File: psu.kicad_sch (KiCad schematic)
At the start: 0 parts

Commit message: First version of analog path, without resistor values
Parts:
- added U16: DAC80504, Package_DFN_QFN:Texas_RTE0016D_WQFN-16-1EP_3x3mm_P0.5mm_EP0.8x0.8mm_ThermalVias, symbol Analog_DAC:DAC80504
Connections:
- new net CH1_GAIN_DAC: U16.2 (OUT0)
- new net CH1_OFFSET_DAC: U16.4 (OUT2)
- new net CH2_GAIN_DAC: U16.3 (OUT1)
- new net CH2_OFFSET_DAC: U16.5 (OUT3)

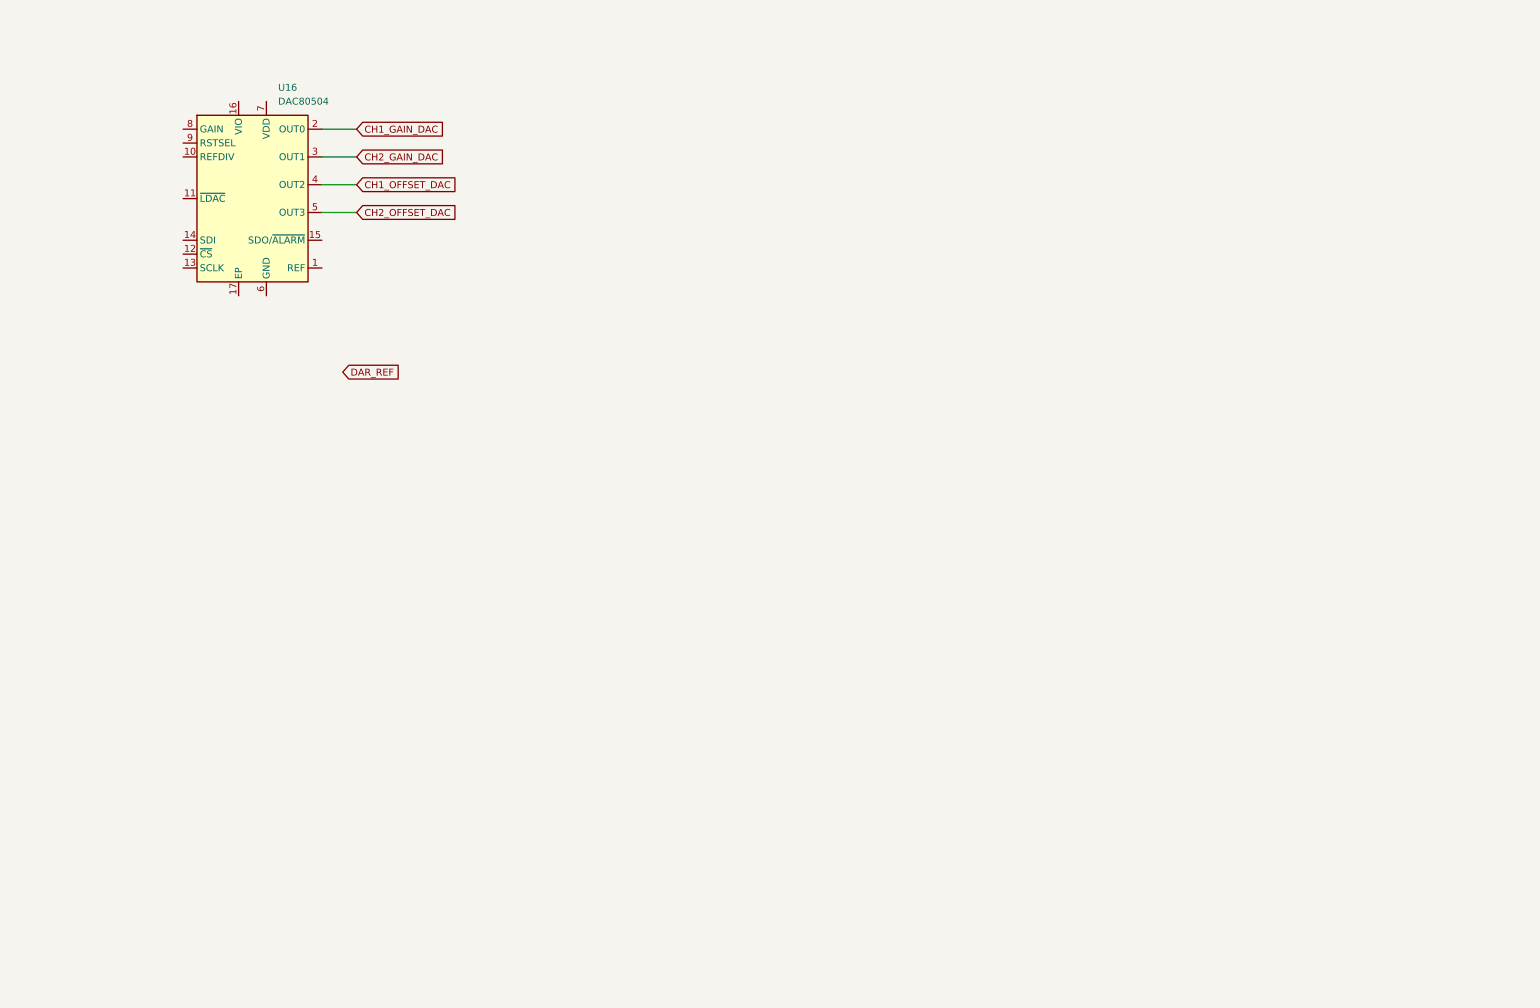
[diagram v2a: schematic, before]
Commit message: Touch up analog front end, add base of the psu
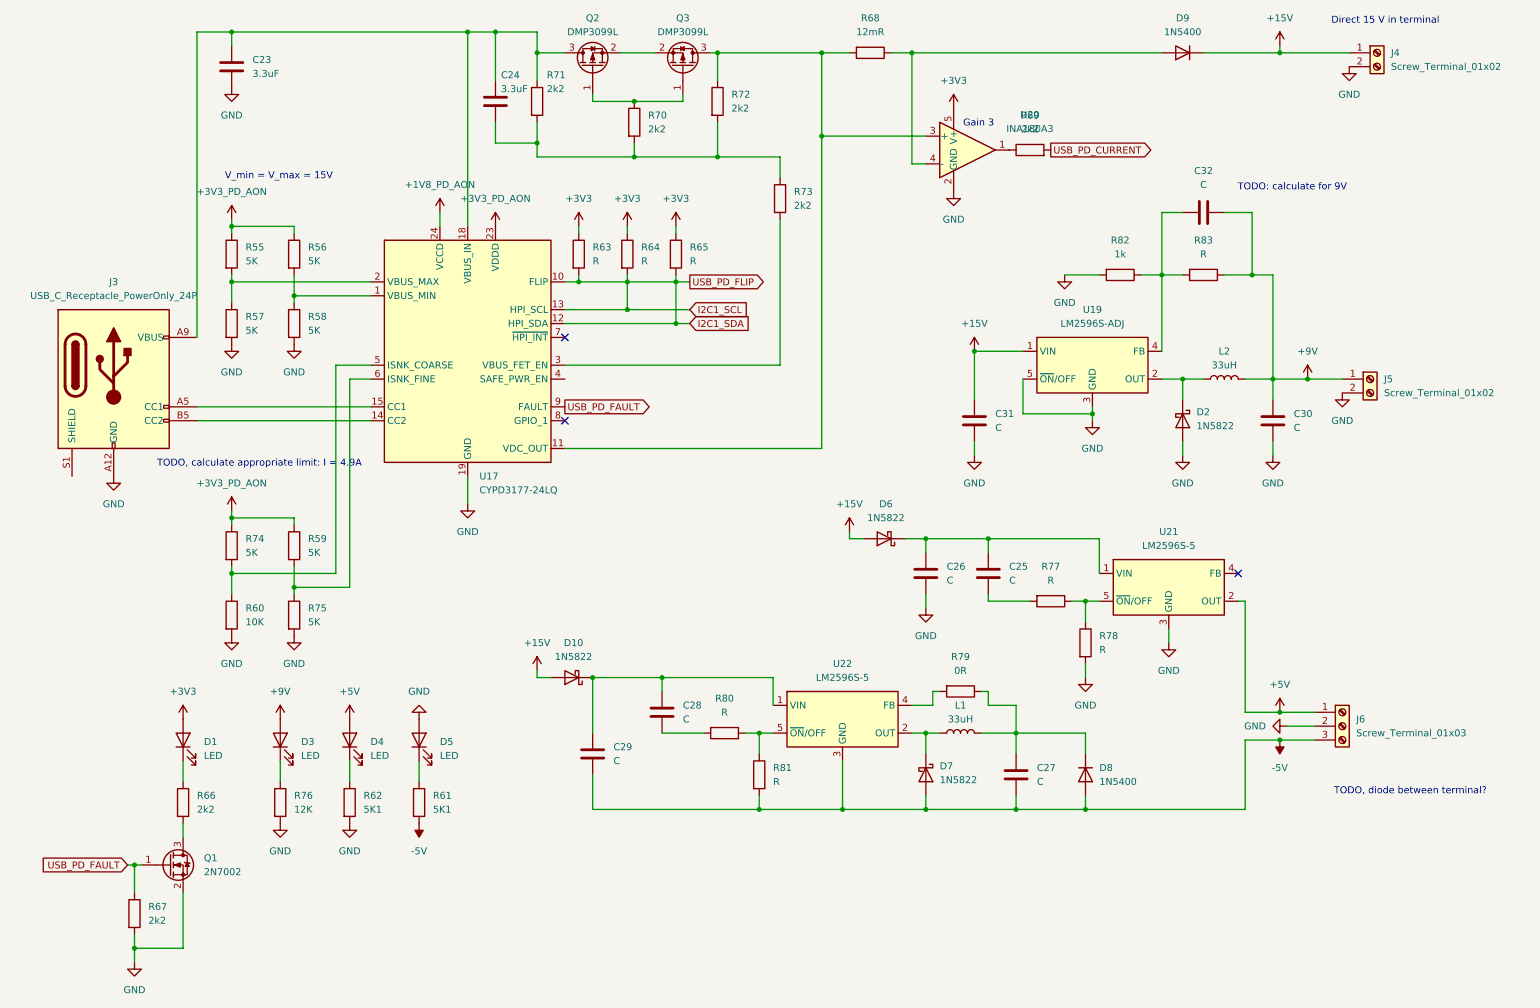
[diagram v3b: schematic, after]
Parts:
- removed U16: DAC80504, Package_DFN_QFN:Texas_RTE0016D_WQFN-16-1EP_3x3mm_P0.5mm_EP0.8x0.8mm_ThermalVias, symbol Analog_DAC:DAC80504
- added C23, C24: 3.3uF, symbol Device:C
- added C25, C26, C27, C28, C29, C30, C31, C32: C, symbol Device:C
- added D1, D3, D4, D5: LED, symbol Device:LED
- added D10, D2, D6, D7: 1N5822, Diode_THT:D_DO-201AD_P15.24mm_Horizontal, symbol Diode:1N5822
- added D8, D9: 1N5400, Diode_THT:D_DO-201AD_P15.24mm_Horizontal, symbol Diode:1N5400
- added J3: USB_C_Receptacle_PowerOnly_24P, symbol Connector:USB_C_Receptacle_PowerOnly_24P
- added J4, J5: Screw_Terminal_01x02, symbol Connector:Screw_Terminal_01x02
- added J6: Screw_Terminal_01x03, symbol Connector:Screw_Terminal_01x03
- added L1, L2: 33uH, symbol Device:L
- added Q1: 2N7002, Package_TO_SOT_SMD:SOT-23, symbol Transistor_FET:2N7002
- added Q2, Q3: DMP3099L, Package_TO_SOT_SMD:SOT-23, symbol Transistor_FET:DMP3099L
- added R55, R56, R57, R58, R59, R74, R75: 5K, symbol Device:R
- added R60: 10K, symbol Device:R
- added R61, R62: 5K1, symbol Device:R
- added R63, R64, R65, R77, R78, R80, R81, R83: R, symbol Device:R
- added R66, R67, R69, R70, R71, R72, R73: 2k2, symbol Device:R
- added R68: 12mR, symbol Device:R
- added R76: 12K, symbol Device:R
- added R79: 0R, symbol Device:R
- added R82: 1k, symbol Device:R
- added U17: CYPD3177-24LQ, Package_DFN_QFN:QFN-24-1EP_4x4mm_P0.5mm_EP2.75x2.75mm, symbol Interface_USB:CYPD3177-24LQ
- added U19: LM2596S-ADJ, Package_TO_SOT_SMD:TO-263-5_TabPin3, symbol Regulator_Switching:LM2596S-ADJ
- added U20: INA180A3, Package_TO_SOT_SMD:SOT-23-5, symbol Amplifier_Current:INA180A3
- added U21, U22: LM2596S-5, Package_TO_SOT_SMD:TO-263-5_TabPin3, symbol Regulator_Switching:LM2596S-5
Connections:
- new net: D5.1 (K), R61.1
- new net: C24.2, R70.2, R71.2, R72.2, R73.1
- new net: R73.2, U17.3 (VBUS_FET_EN)
- new net: D9.2 (A), R68.1, U20.4 (-)
- new net: C23.1, C24.1, J3.A4 (VBUS), J3.A9 (VBUS), J3.B4 (VBUS), J3.B9 (VBUS), Q2.3 (D), R71.1, U17.18 (VBUS_IN)
- new net: J3.A5 (CC1), U17.15 (CC1)
- new net: J3.B5 (CC2), U17.14 (CC2)
- new net: R59.2, R75.1, U17.6 (ISNK_FINE)
- new net: Q2.1 (G), Q3.1 (G), R70.1
- new net: Q3.3 (D), R68.2, R72.1, U17.11 (VDC_OUT), U20.3 (+)
- new net: R56.2, R58.1, U17.1 (VBUS_MIN)
- new net: D7.1 (K), L1.1, U22.2 (OUT)
- new net: C27.1, D8.1 (K), L1.2, R79.1
- new net: D1.1 (K), R66.1
- new net: D2.1 (K), L2.1, U19.2 (OUT)
- new net: C32.2, R82.1, R83.2, U19.4 (FB)
- new net: C25.1, C26.1, D6.1 (K), U21.1 (VIN)
- new net: D3.1 (K), R76.1
- new net: Q2.2 (S), Q3.2 (S)
- new net: Q1.3 (D), R66.2
- new net: R60.1, R74.2, U17.5 (ISNK_COARSE)
- new net: R55.2, R57.1, U17.2 (VBUS_MAX)
- new net: R77.1, R78.1, U21.5 (~{ON}/OFF)
- new net: C25.2, R77.2
- new net: R79.2, U22.4 (FB)
- new net: R80.1, R81.1, U22.5 (~{ON}/OFF)
- new net: D4.1 (K), R62.1
- new net: C28.1, C29.1, D10.1 (K), U22.1 (VIN)
- new net: C28.2, R80.2
- new net: R69.1, U20.1
- new net +15V: C31.1, D10.2 (A), D6.2 (A), D9.1 (K), J4.1 (Pin_1), U19.1 (VIN)
- new net +1V8_PD_AON: U17.24 (VCCD)
- new net +3V3: D1.2 (A), R63.1, R64.1, R65.1, U20.5 (V+)
- new net +3V3_PD_AON: R55.1, R56.1, R59.1, R74.1, U17.23 (VDDD)
- new net +5V: D4.2 (A), J6.1 (Pin_1), U21.2 (OUT)
- new net +9V: C30.1, C32.1, D3.2 (A), J5.1 (Pin_1), L2.2, R83.1
- new net -5V: C27.2, C29.2, D7.2 (A), D8.2 (A), J6.3 (Pin_3), R61.2, R81.2, U22.3 (GND)
- new net GND: C23.2, C26.2, C30.2, C31.2, D2.2 (A), D5.2 (A), J3.A1 (GND), J3.A12 (GND), J3.B1 (GND), J3.B12 (GND), J4.2 (Pin_2), J5.2 (Pin_2), J6.2 (Pin_2), Q1.2 (S), R57.2, R58.2, R60.2, R62.2, R67.2, R75.2, R76.2, R78.2, R82.2, U17.19 (GND), U17.22 (GND), U17.25 (GND), U19.3 (GND), U19.5 (~{ON}/OFF), U20.2 (GND), U21.3 (GND)
- new net I2C1_SCL: R63.2, R64.2, R65.2, U17.10 (FLIP), U17.12 (HPI_SDA), U17.13 (HPI_SCL)
- new net USB_PD_CURRENT: R69.2
- new net USB_PD_FAULT: Q1.1 (G), R67.1, U17.9 (FAULT)
- no-connect marks 0 -> 3
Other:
- note added: "Direct 15 V in terminal"
- note added: "Gain 3"
- note added: "TODO, calculate appropriate limit: I = 4.9A"
- note added: "TODO, diode between terminal?"
- note added: "TODO: calculate for 9V"
- note added: "V_min = V_max = 15V"

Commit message: Save work on simplifying the desing
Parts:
- removed C23, C24: 3.3uF, symbol Device:C
- removed C25, C26, C27, C28, C29, C30, C31, C32: C, symbol Device:C
- removed D1: LED, symbol Device:LED
- removed D10, D2, D6, D7: 1N5822, Diode_THT:D_DO-201AD_P15.24mm_Horizontal, symbol Diode:1N5822
- removed D8, D9: 1N5400, Diode_THT:D_DO-201AD_P15.24mm_Horizontal, symbol Diode:1N5400
- removed J3: USB_C_Receptacle_PowerOnly_24P, symbol Connector:USB_C_Receptacle_PowerOnly_24P
- removed J5: Screw_Terminal_01x02, symbol Connector:Screw_Terminal_01x02
- removed J6: Screw_Terminal_01x03, symbol Connector:Screw_Terminal_01x03
- removed L1, L2: 33uH, symbol Device:L
- removed Q1: 2N7002, Package_TO_SOT_SMD:SOT-23, symbol Transistor_FET:2N7002
- removed Q2, Q3: DMP3099L, Package_TO_SOT_SMD:SOT-23, symbol Transistor_FET:DMP3099L
- removed R55, R56, R57, R58, R59, R74, R75: 5K, symbol Device:R
- removed R60: 10K, symbol Device:R
- removed R63, R64, R65, R77, R78, R80, R81, R83: R, symbol Device:R
- removed R66, R67, R69, R70, R71, R72, R73: 2k2, symbol Device:R
- removed R68: 12mR, symbol Device:R
- removed R79: 0R, symbol Device:R
- removed R82: 1k, symbol Device:R
- removed U17: CYPD3177-24LQ, Package_DFN_QFN:QFN-24-1EP_4x4mm_P0.5mm_EP2.75x2.75mm, symbol Interface_USB:CYPD3177-24LQ
- removed U19: LM2596S-ADJ, Package_TO_SOT_SMD:TO-263-5_TabPin3, symbol Regulator_Switching:LM2596S-ADJ
- removed U20: INA180A3, Package_TO_SOT_SMD:SOT-23-5, symbol Amplifier_Current:INA180A3
- removed U21, U22: LM2596S-5, Package_TO_SOT_SMD:TO-263-5_TabPin3, symbol Regulator_Switching:LM2596S-5
- added J3: Screw_Terminal_01x03, symbol Connector:Screw_Terminal_01x03
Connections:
- net +5V: now also J3.1 (Pin_1)
- net -5V: now also J3.3 (Pin_3)
- net GND: now also J3.2 (Pin_2)
- net +15V renamed +12V
- no-connect marks 3 -> 0
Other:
- note added: "+5V / -5V"
- note added: "12V"
- note removed: "Direct 15 V in terminal"
- note removed: "Gain 3"
- note removed: "TODO, calculate appropriate limit: I = 4.9A"
- note removed: "TODO, diode between terminal?"
- note removed: "TODO: calculate for 9V"
- note removed: "V_min = V_max = 15V"
- moved on the sheet: D3, D4, D5, R61, R62, R76

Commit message: Simplifying the design
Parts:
- added C24, C27, C28, C29, C51: C, symbol Device:C
- added C25, C30, C31, C32, C52: 10uF, symbol Device:C
- added C26, C48, C49, C50, C53: 22uF, symbol Device:C
- added R50: 120, symbol Device:R
- added R52: 560, symbol Device:R
- added R65, R66, R67, R68, R69, R70, R71, R72: R, symbol Device:R
- added U15, U17, U18, U19, U20: AP1117-ADJ, Package_TO_SOT_SMD:SOT-223-3_TabPin2, symbol Regulator_Linear:AP1117-ADJ
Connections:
- net +12V: now also D3.2 (A)
- net +5V: now also C27.1, C28.1, C29.1, C30.1, C31.1, C32.1, C51.1, C52.1, U17.3 (VI), U18.3 (VI), U19.3 (VI), U20.3 (VI)
- net +9V: now also C24.1, C25.1, U15.3 (VI); no longer D3.2 (A)
- net GND: now also C24.2, C25.2, C26.2, C27.2, C28.2, C29.2, C30.2, C31.2, C32.2, C48.2, C49.2, C50.2, C51.2, C52.2, C53.2, R52.2, R66.2, R68.2, R70.2, R72.2
- new net: R69.2, R70.1, U19.1 (ADJ)
- new net: C50.1, R69.1, U19.2 (VO)
- new net: C53.1, R71.1, U20.2 (VO)
- new net: R71.2, R72.1, U20.1 (ADJ)
- new net: R67.2, R68.1, U18.1 (ADJ)
- new net: C26.1, R50.1, U15.2 (VO)
- new net: C48.1, R65.1, U17.2 (VO)
- new net: R50.2, R52.1, U15.1 (ADJ)
- new net: R65.2, R66.1, U17.1 (ADJ)
- new net: C49.1, R67.1, U18.2 (VO)
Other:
- note added: "TODO: recommended to change for AZ1117C/E"
- moved on the sheet: J3, J4

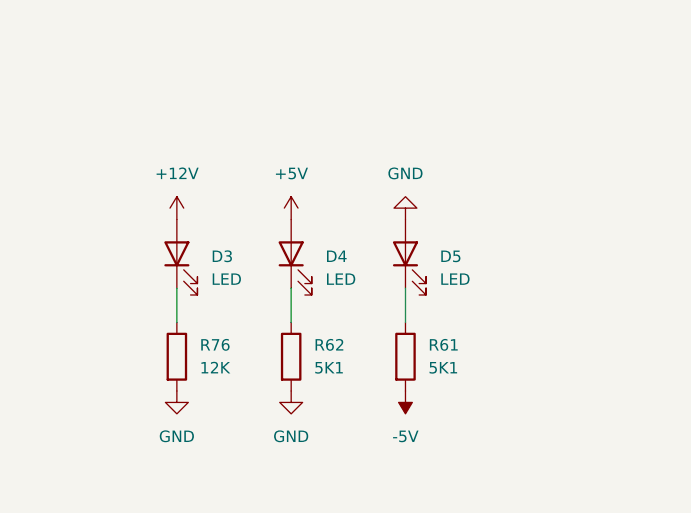
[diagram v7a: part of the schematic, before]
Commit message: Mostly finished schematics, without decoupling and power
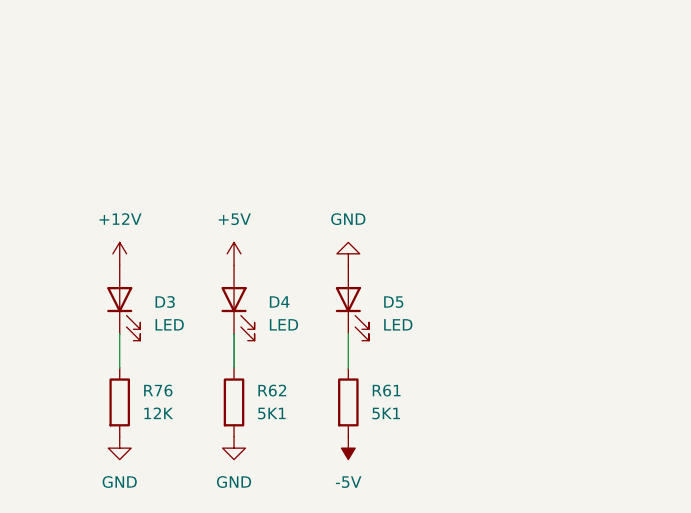
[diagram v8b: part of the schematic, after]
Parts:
- R50, R52, R61, R62, R65, R66, R67, R68, R69, R70, R71, R72, R76: footprint (none) -> Resistor_SMD:R_1206_3216Metric
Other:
- moved on the sheet: D3, D4, D5, R61, R62, R76
